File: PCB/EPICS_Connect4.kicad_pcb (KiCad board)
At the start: 4 copper layers, 50 x 60 mm, 90 parts, among them J1 Power, J2 TC2030, J3 USB_C_Receptacle_USB2.0_14P, J4 EndA, J5 EndB, J6 LEDA, J7 LEDB, J8 Motor, SW1 ESP.RST, SW2 ESP.BOOT, U1 TPS54202DDC, U2 AP2205-5, U3 STM32G474CBTx, U4 SN74AHCT1G125DBVR, U5 SN74AHCT1G125DBVR, U6 ESP32-C3-WROOM-02, U7 USBLC6-2SC6, U8 TMC2209

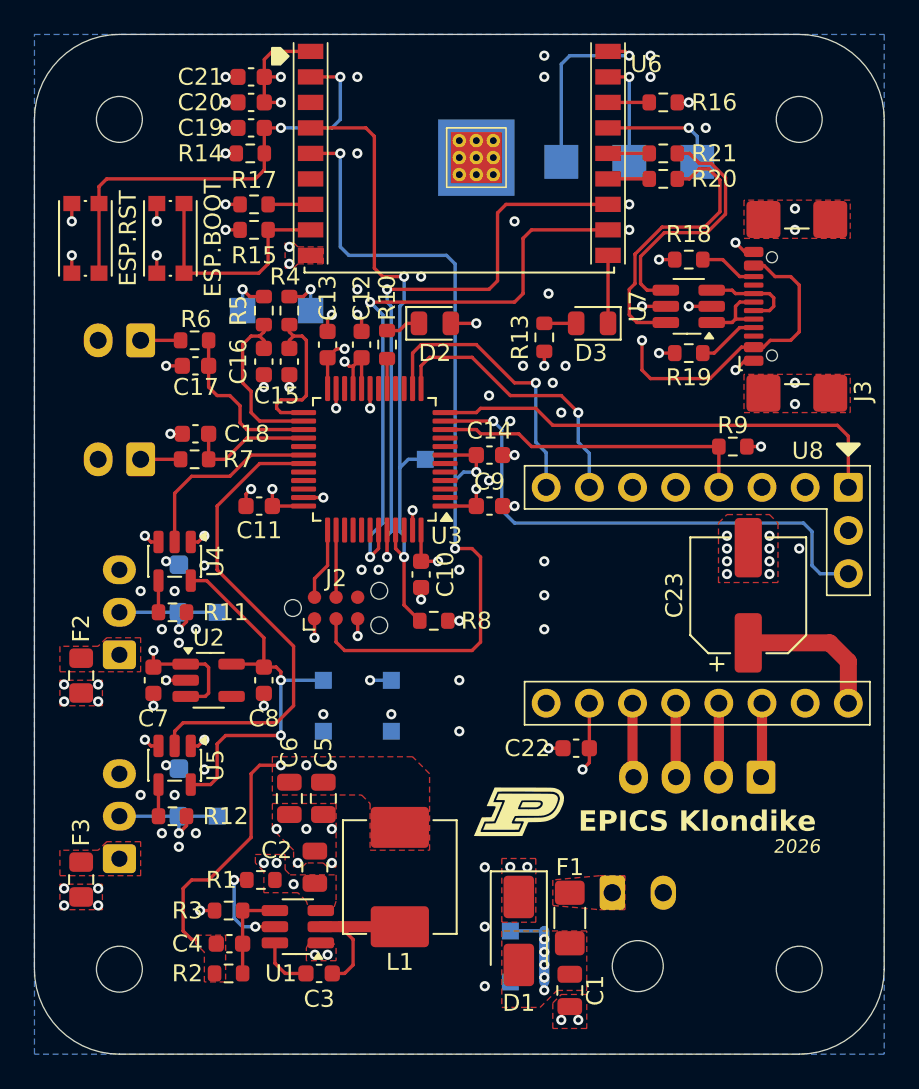
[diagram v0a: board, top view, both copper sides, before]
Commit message: Swap Molex connector 3D model to 43650-0215
Co-Authored-By: Claude Opus 5.5 <noreply@anthropic.com>
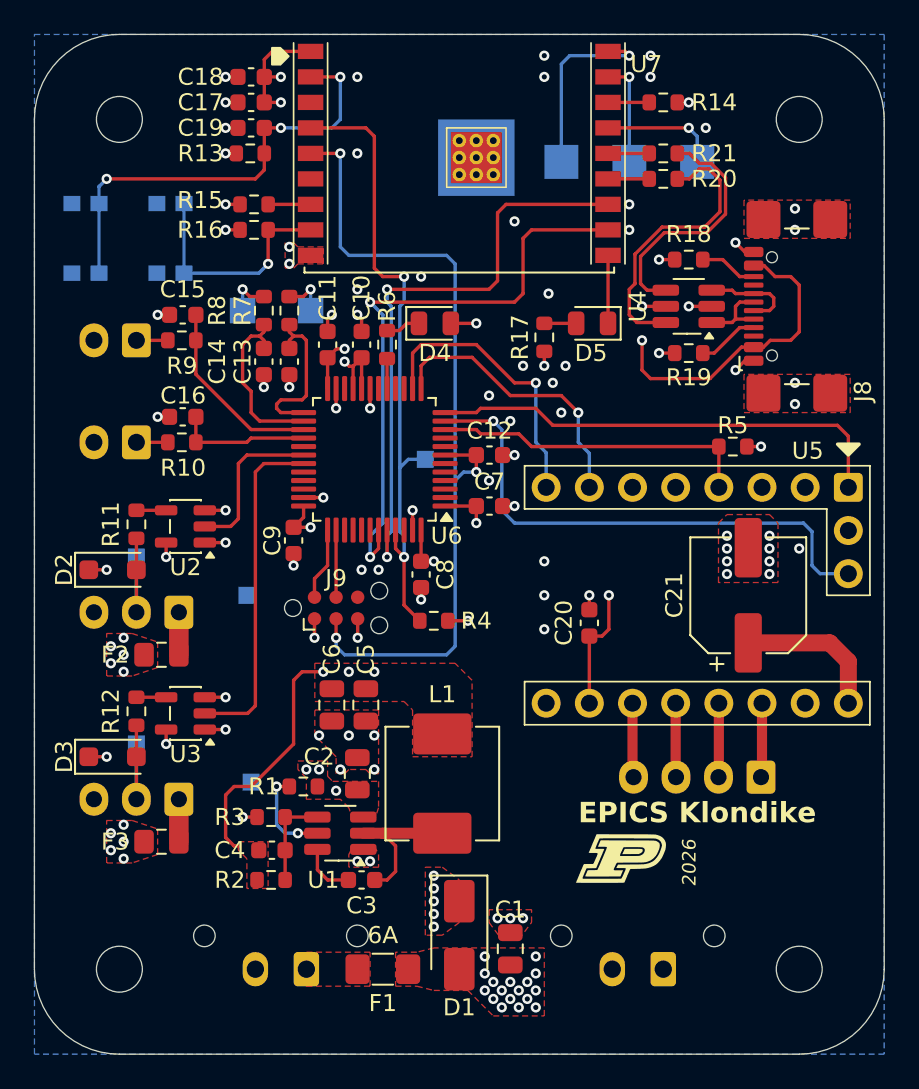
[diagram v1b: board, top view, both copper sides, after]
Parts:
- removed the C7 at (132.0, 113.0)
- removed the C8 at (138.5, 113.0)
- removed the D4 at (133.5, 107.6)
- removed the D5 at (133.5, 119.6)
- removed the TP1 at (153.0, 127.8)
- removed the TP6 at (146.0, 116.0)
- removed the TP8 at (135.8, 109.0)
- removed the TP9 at (135.8, 121.0)
- removed the U4 at (133.2, 106.0)
- removed the U5 at (133.2, 118.0)
- added D2: SMF5.0A, Diode_SMD:D_SOD-123F, F.Cu at (129.6, 106.5)
- added D3: SMF5.0A, Diode_SMD:D_SOD-123F, F.Cu at (129.6, 117.5)
- added J2: +12V, Connector_Molex:Molex_Micro-Fit_3.0_43650-0215_1x02_P3.00mm_Vertical, B.Cu at (162.0, 130.0)
- added U3: SN74AHCT1G125DBVR, Package_TO_SOT_SMD:SOT-23-5, F.Cu at (133.9, 115.0)
- D1: value SMAJ12A -> SMAJ5A
- F1: value 5A -> 6A
- J1: value Power -> +5V; footprint Connector_Molex:Molex_Micro-Fit_3.0_43650-0200_1x02_P3.00mm_Horizontal -> Connector_Molex:Molex_Micro-Fit_3.0_43650-0215_1x02_P3.00mm_Vertical
- J7: renamed from J8; value Motor -> MOTOR
- SW1, SW2: moved to B.Cu
- TP3: value +5V -> DataA
- TP5: value +3V3 -> DataB
- U2: value AP2205-5 -> SN74AHCT1G125DBVR; footprint Package_TO_SOT_SMD:SOT-23-5_HandSoldering -> Package_TO_SOT_SMD:SOT-23-5
- moved TP2 27.5 mm to (137.5, 108.0)
- moved J1 18.6 mm to (141.0, 130.0), turned to 180 degrees
- moved TP5 15.5 mm to (131.0, 116.8)
- moved TP3 13.2 mm to (131.0, 105.8)
- moved F1 11.4 mm to (145.5, 130.0), turned to 0 degrees
- moved U2 9.15 mm to (133.9, 104.0), turned to 180 degrees
- moved C20 7.42 mm to (157.7, 109.6), turned to -90 degrees
- moved SYM1 6.60 mm to (159.5, 123.5)
- moved R12 6.53 mm to (131.0, 114.8), turned to -90 degrees
- moved C2 6.04 mm to (144.0, 118.5)
- moved C3 6.04 mm to (144.2, 124.8)
- moved C4 6.04 mm to (139.0, 123.0)
- moved C5 6.04 mm to (144.5, 114.5)
- moved C6 6.04 mm to (142.5, 114.5)
- moved L1 6.04 mm to (149.0, 119.1)
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- renumbered C12 to C10, C13 to C11, C14 to C12, C15 to C13, C16 to C14, C17 to C15, C18 to C16, C20 to C17, C21 to C18, C22 to C20, C23 to C21, C9 to C7, C10 to C8, C11 to C9, D2 to D4, D3 to D5, J4 to J3, J5 to J4, J6 to J5, J7 to J6, J3 to J8, J2 to J9, R7 to R10, R14 to R13, R16 to R14, R17 to R15, R15 to R16, R13 to R17, R8 to R4, R9 to R5, R10 to R6, R4 to R7, R5 to R8, R6 to R9, TP7 to TP1, TP11 to TP10, TP12 to TP6, TP13 to TP7, TP14 to TP8, TP10 to TP9, U7 to U4, U8 to U5, U3 to U6, U6 to U7
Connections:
- C1 pad 1: +12V -> +5V
- C2 pad 2: +12V -> +5V
- D1 pad 2: +12V -> +5V
- F1 pad 2: +12V -> +5V
- F2 pad 1: +12V -> +5V
- F3 pad 1: +12V -> +5V
- R1 pad 1: +12V -> +5V
- R11 pad 1: Net-(U4-Y) -> Net-(U2-Y)
- TP3 pad 1: +5V -> /STM32 Controller/ledDataA
- TP5 pad 1: +3V3 -> /STM32 Controller/ledDataB
- U1 pad 3: +12V -> +5V
- U2 pad 1: +12V -> GND
- U2 pad 2: GND -> /STM32 Controller/LED.A
- U2 pad 3: +12V -> GND
- U2 pad 4: unconnected-(U2-NC-Pad4) -> Net-(U2-Y)
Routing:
- net +5V: track 24.2 -> 1.70 mm, vias 2 -> 32
- net +12V: track 21.1 -> 8.80 mm, vias 17 -> 0
- net /STM32 Controller/LED.B: track 28.2 -> 20.0 mm
- net GND: track 35.1 -> 31.5 mm, vias 110 -> 87
- net Net-(J6-Pin_1): track 0.00 -> 2.50 mm
- net Net-(J5-Pin_1): track 0.00 -> 2.50 mm
- net /STM32 Controller/NRST: track 52.4 -> 50.2 mm
- net /STM32 Controller/LED.A: track 11.4 -> 9.46 mm
- net Net-(U4-Y): track 1.86 -> 0.00 mm
- net Net-(U2-Y): track 0.00 -> 1.75 mm
- net +3V3: track 50.4 -> 51.8 mm, vias 20 -> 19
- net /STM32 Controller/END.A*: track 9.96 -> 11.2 mm
- net /STM32 Controller/END.B: track 2.35 -> 1.85 mm
- net /STM32 Controller/END.A: track 2.35 -> 1.85 mm
- net /STM32 Controller/ledDataB: track 7.94 -> 7.60 mm, vias 1 -> 0
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- added copper zone on F.Cu, net +5V
- added copper zone on In2.Cu, net +5V
- removed copper zone on F.Cu, net +12V
- removed copper zone on F.Cu, net Net-(J5-Pin_1)
- removed copper zone on F.Cu, net Net-(J6-Pin_1)
